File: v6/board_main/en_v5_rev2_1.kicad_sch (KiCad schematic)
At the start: 7 parts, among them J1 M50-3142045THT, J2 M50-3142045THT, J3 53261-0271, J4 USB4105-GF-A

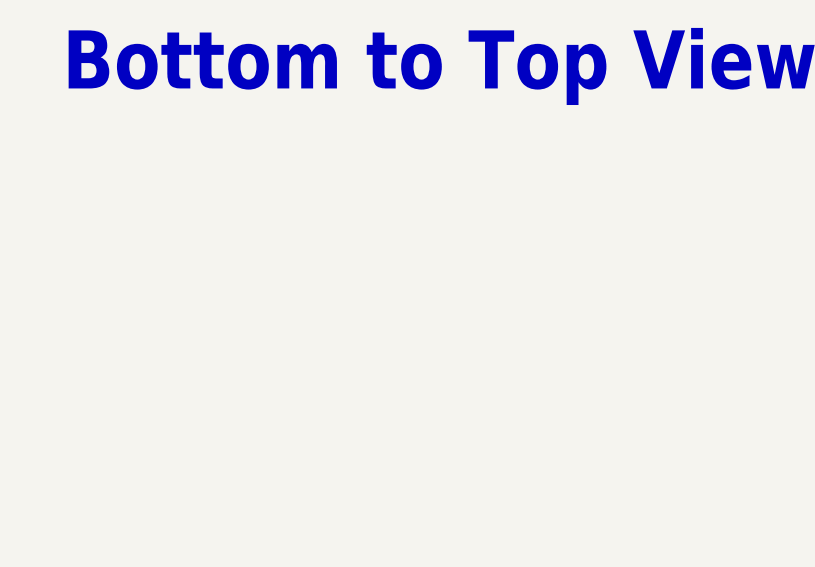
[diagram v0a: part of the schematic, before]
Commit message: Rephrasing ENV5 design
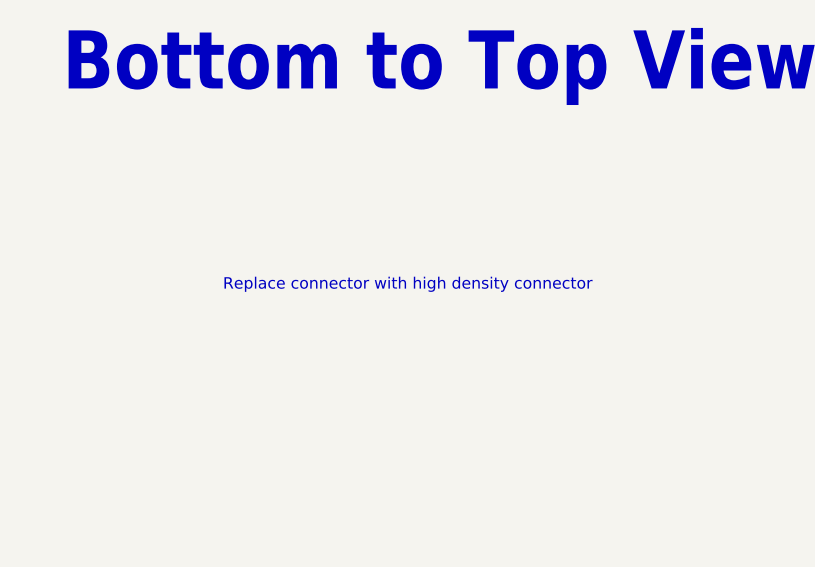
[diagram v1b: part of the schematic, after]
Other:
- note added: "Replace connector with high density connector"
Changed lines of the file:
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@@
+		)
+	)
+	(text "Replace connector with high density connector"
+		(exclude_from_sim no)
+		(at 143.764 60.198 0)
+		(effects
+			(font
+				(size 1.27 1.27)
+			)
 		)
 	)
